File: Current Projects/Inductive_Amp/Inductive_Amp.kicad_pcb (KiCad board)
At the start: 2 copper layers, 10 parts, among them J1 Conn_01x03, J2 Conn_01x03, U1 NA555D, U2 74LS14, U3 TLV2372

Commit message: Inductive PCB!
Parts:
- added C3: 0.1u, Capacitor_SMD:C_0805_2012Metric, F.Cu at (128.3, 88.9)
- added C4: 1u, Capacitor_SMD:C_0805_2012Metric, F.Cu at (130.8, 88.9)
- added C5: 1u, Capacitor_SMD:C_0805_2012Metric, F.Cu at (169.5, 87.9)
- added C6: 0.1u, Capacitor_SMD:C_0805_2012Metric, F.Cu at (172.1, 87.9)
- added C7: 0.1u, Capacitor_SMD:C_0805_2012Metric, F.Cu at (163.5, 83.8)
- added C8: 0.1u, Capacitor_SMD:C_0805_2012Metric, F.Cu at (154.4, 94.6)
- added C9: 0.1u, Capacitor_SMD:C_0805_2012Metric, F.Cu at (137.9, 91.2)
- added D1: PESD5V0S2BT, Package_TO_SOT_SMD:SOT-23-3, F.Cu at (125.5, 85.7)
- added D2: PESD5V0S2BT, Package_TO_SOT_SMD:SOT-23-3, F.Cu at (175.1, 85.7)
- added H1: M2, MountingHole:MountingHole_2.2mm_M2_DIN965_Pad, F.Cu at (128.3, 78.7)
- added H2: M2, MountingHole:MountingHole_2.2mm_M2_DIN965_Pad, F.Cu at (128.3, 95.2)
- added H3: M2, MountingHole:MountingHole_2.2mm_M2_DIN965_Pad, F.Cu at (172.1, 78.7)
- added H4: M2, MountingHole:MountingHole_2.2mm_M2_DIN965_Pad, F.Cu at (172.1, 95.2)
- added R4: 1k, Resistor_SMD:R_0805_2012Metric, F.Cu at (131.0, 84.5)
- added R5: 1k, Resistor_SMD:R_0805_2012Metric, F.Cu at (168.6, 82.4)
- J1: value Conn_01x03 -> INPUT
- J2: value Conn_01x03 -> OUTPUT
- R2: value 1k -> 15k
- R3: value 200 -> 10k
- moved R3 7.90 mm to (135.8, 79.9), turned to 180 degrees
- moved J2 7.14 mm to (179.1, 84.5)
- moved J1 5.74 mm to (121.3, 84.5)
- moved R2 5.49 mm to (140.2, 81.7)
- moved R1 2.89 mm to (165.7, 87.4), turned to 180 degrees
- moved U2 2.05 mm to (149.6, 89.5), turned to -90 degrees
- moved C1 1.69 mm to (165.7, 89.7)
- moved C2 1.18 mm to (162.9, 92.7), turned to 0 degrees
- moved U3 0.41 mm to (136.0, 85.1), turned to -90 degrees
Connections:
- U1 pad 3: /OUT -> Net-(U1-Q)
- U2 pad 1: Net-(U2-Pad1) -> Net-(R2-Pad2)
- U2 pad 10: (no net) -> unconnected-(U2-Pad10)
- U2 pad 11: (no net) -> +5V
- U2 pad 12: (no net) -> unconnected-(U2-Pad12)
- U2 pad 13: (no net) -> +5V
- U2 pad 3: Net-(R2-Pad2) -> +5V
- U2 pad 4: Net-(U2-Pad1) -> unconnected-(U2-Pad4)
- U2 pad 5: (no net) -> +5V
- U2 pad 6: (no net) -> unconnected-(U2-Pad6)
- U2 pad 8: (no net) -> unconnected-(U2-Pad8)
- U2 pad 9: (no net) -> +5V
- U3 pad 3: /Vin -> Net-(U3A-+)
- U3 pad 4: (no net) -> GND
- U3 pad 5: (no net) -> GND
- U3 pad 6: (no net) -> Net-(U3B--)
- U3 pad 7: (no net) -> Net-(U3B--)
- U3 pad 8: (no net) -> +5V
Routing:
- net +5V: track 0.00 -> 103.1 mm, vias 0 -> 2
- net Net-(R2-Pad2): track 0.00 -> 19.9 mm
- net Net-(U1-Q): track 0.00 -> 14.8 mm
- net /OUT: track 0.00 -> 10.6 mm
- net /Vin: track 0.00 -> 9.03 mm
- net Net-(U1-TR): track 0.00 -> 6.76 mm
- net Net-(U3A--): track 0.00 -> 6.64 mm
- net Net-(U1-DIS): track 0.00 -> 6.42 mm
- net Net-(U3A-+): track 0.00 -> 5.05 mm
- net Net-(U1-CV): track 0.00 -> 2.83 mm
- net Net-(U3B--): track 0.00 -> 1.27 mm
- net GND: vias 0 -> 116
- added copper zone on B.Cu, net GND
- added copper zone on F.Cu, net GND
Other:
- board outline added: 64.1 x 25.4 mm
- board text added: "IN"
- board text added: "NCSU Baja 2026"
- board text added: "OUT"
- board text added: "RPM Input Conditioning"

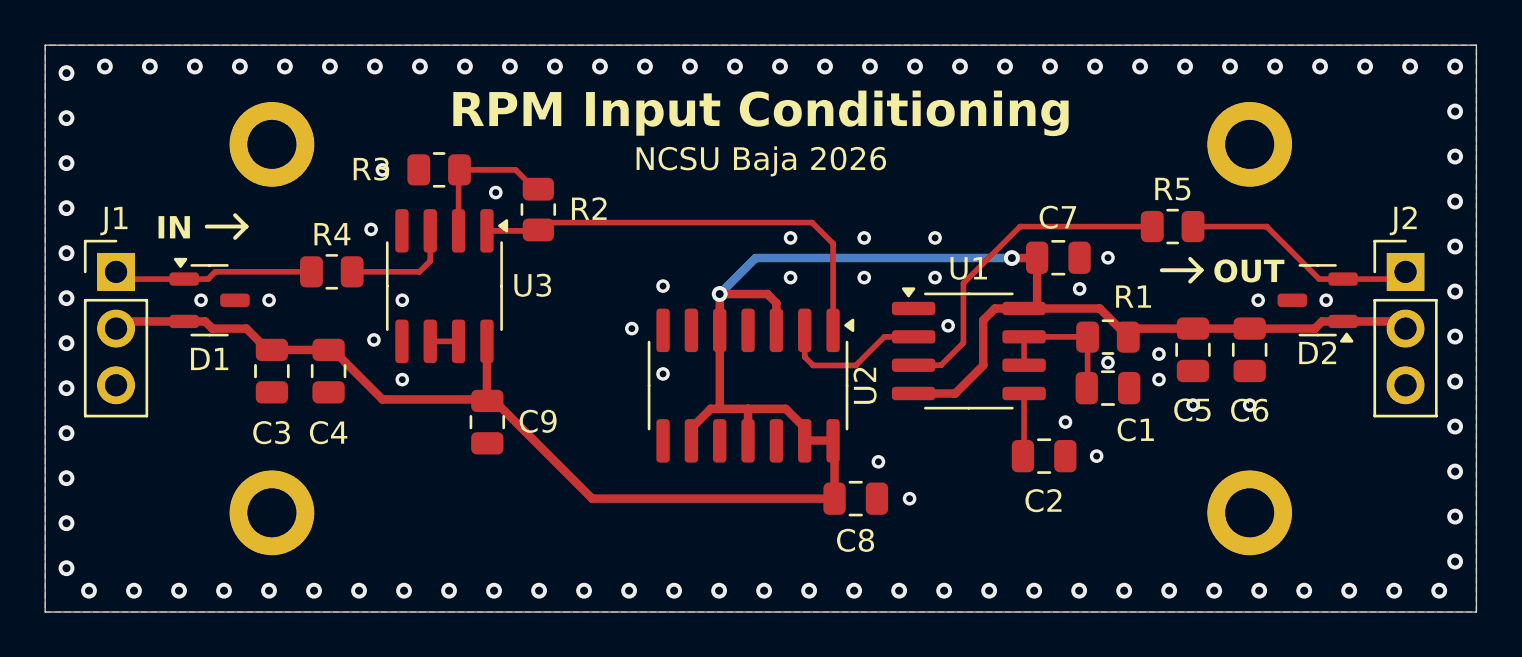
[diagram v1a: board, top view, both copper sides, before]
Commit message: Inductive PCB pull down R
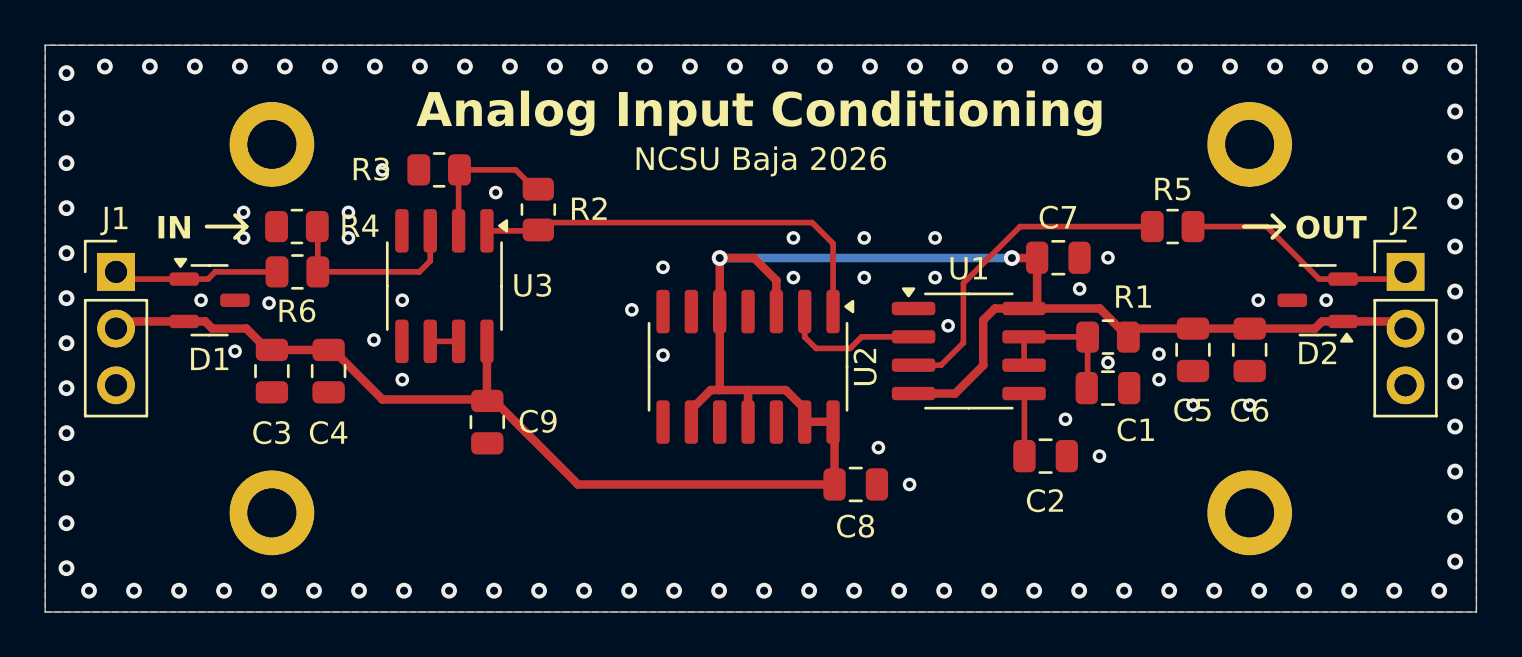
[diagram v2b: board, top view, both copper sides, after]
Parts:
- added R6: 1M, Resistor_SMD:R_0805_2012Metric, F.Cu at (129.4, 82.4)
- moved R4 1.54 mm to (129.4, 84.5)
- moved U2 0.84 mm to (149.6, 88.7)
- moved C8 0.63 mm to (154.4, 94.0)
- moved C2 0.07 mm to (162.9, 92.7)
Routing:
- net Net-(U3A-+): track 5.05 -> 8.64 mm
- net /Vin: track 9.03 -> 7.48 mm
- net Net-(R2-Pad2): track 19.9 -> 19.1 mm
- net +5V: track 103.1 -> 103.6 mm
- net GND: vias 116 -> 120
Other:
- board text added: "Analog Input Conditioning"
- board text removed: "RPM Input Conditioning"

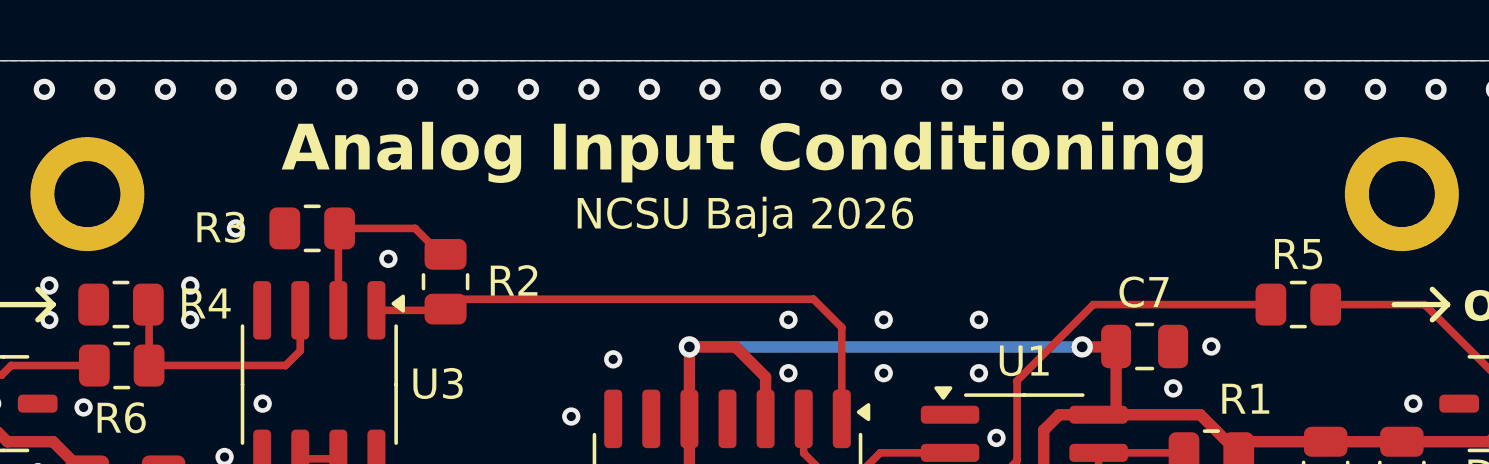
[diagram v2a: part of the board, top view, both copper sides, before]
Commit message: Inductive sch annotations and silkscreen name change
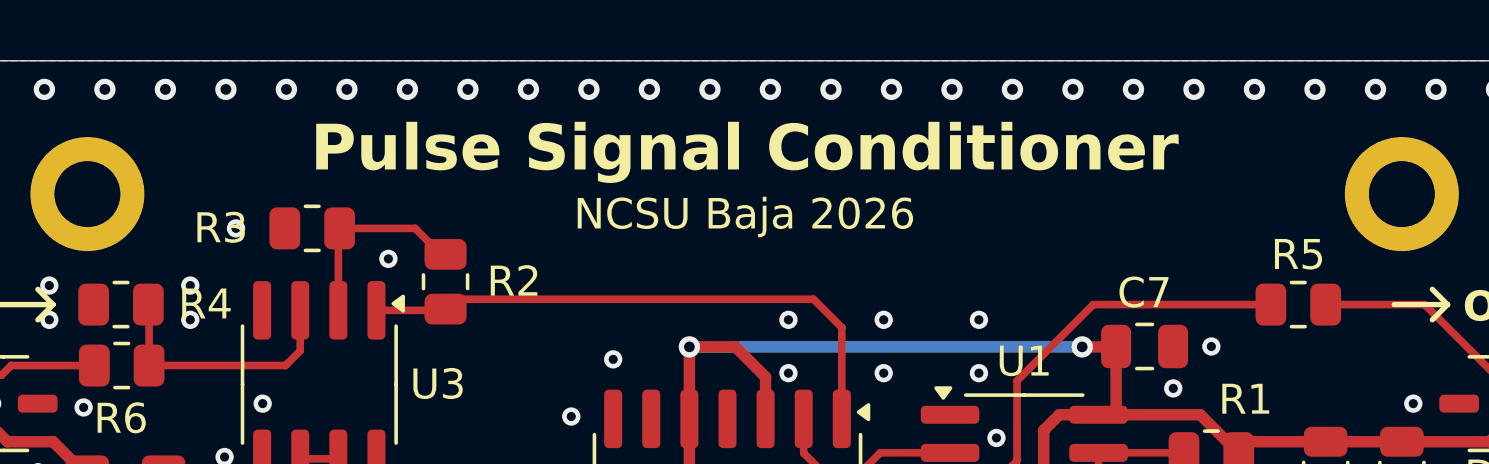
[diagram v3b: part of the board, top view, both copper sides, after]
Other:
- board text added: "Pulse Signal Conditioner"
- board text removed: "Analog Input Conditioning"

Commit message: Final inductive amp!
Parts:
- moved C7 1.40 mm to (164.6, 84.7), turned to 90 degrees
- moved C8 1.39 mm to (153.4, 94.9), turned to -90 degrees
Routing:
- net +5V: track 103.6 -> 92.1 mm, vias 2 -> 0
- net GND: vias 120 -> 128
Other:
- board text added: "Out 5V GND"
- board text added: "Vin 5V GND"
